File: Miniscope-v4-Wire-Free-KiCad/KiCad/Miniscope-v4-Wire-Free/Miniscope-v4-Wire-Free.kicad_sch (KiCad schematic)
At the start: 116 parts, among them J1 0475710001, J10 Conn_01x01, J11 Conn_01x01, J12 Conn_01x01, J14 Conn_01x01, J15 Conn_01x01, J16 Conn_01x01, J17 Conn_01x01, J18 Conn_01x01, J19 Conn_01x01, J2 Conn_01x04, J20 Conn_01x01, J21 Conn_01x01, J22 Conn_01x01, J23 Conn_01x01, J24 Conn_01x01, J25 Conn_01x01, J26 Conn_01x01, J27 Conn_01x01, J3 Conn_01x04, J4 Conn_01x01, J5 Conn_01x01, J6 Conn_01x01, J7 Conn_01x01, J8 Conn_01x01, J9 Conn_01x01, Q1 NTK3134NT1G, Q2 MMBT3904LP-7B, SW1 TL3780AF330QG, U1 LTC3554, U2 HV892, U3 LTC3218, U4 MAX13030EETE+BGA, U5 TSOP57438TT1, U6 ATSAMD51J20A-UUT-EFP, U7 NCP163AMX330TBG, U8 NOIP1SN0480A, U9 LMV321IDCKR, Y2 Crystal

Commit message: Update public repository
- Made copy to a public repository
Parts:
- removed C?: 1u, .Capacitor:C_0201_0603Metric_L, symbol .Device:C_Small
- R22: renamed from R?; footprint .Resistor:R_0201_0603Metric_ERJ_L -> Resistor:R_0201_0603Metric_ERJ_L

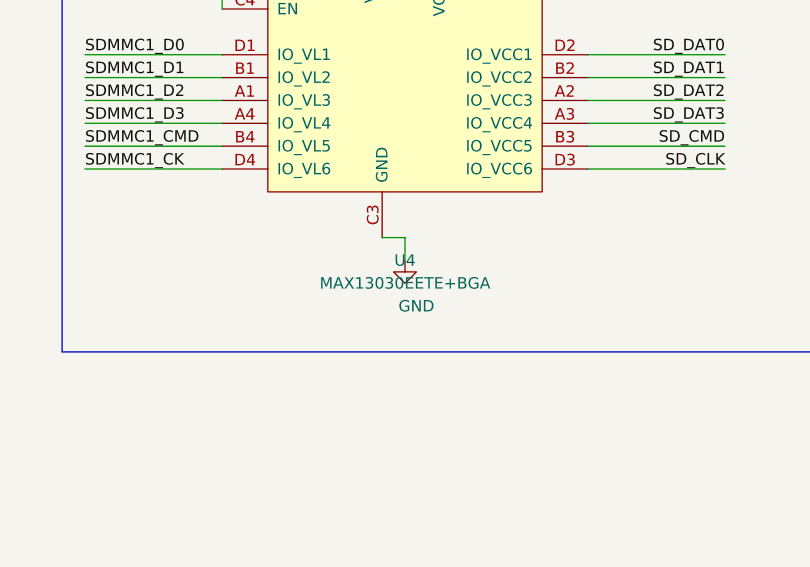
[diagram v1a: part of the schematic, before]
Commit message: Microchip Studio project reorganization, updates to the notebooks
- Reorganized the firmware repository. Now the project can be correctly reconfigured using Atmel Start and the clock settings is correct.

- Added a scan feature for the EWL. By setting a flag on the Set Parameters notebook the user can test different planes to check which one focuses better. More information on how to use this feature can be found soon on the Wire-Free wiki page.

- Added more information to the KiCad project for the batch assembly.

To do:

- Do a final cleaning of the firmware code. See if it's worth moving the ADMA and SDHC specific functions to a custom file
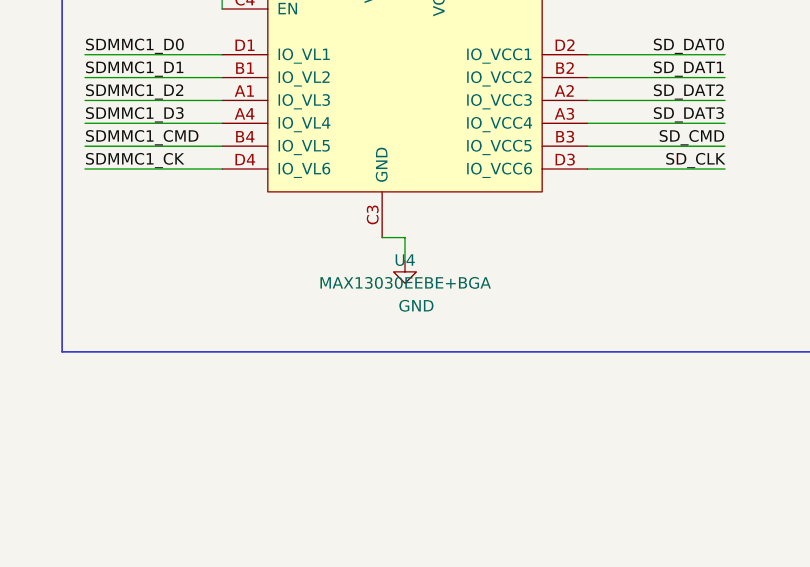
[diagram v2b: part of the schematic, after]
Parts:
- U4: value MAX13030EETE+BGA -> MAX13030EEBE+BGA
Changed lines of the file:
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@@
       (effects (font (size 1.27 1.27)))
     )
-    (property "Value" "MAX13030EETE+BGA" (at 473.71 336.55 0)
+    (property "Value" "MAX13030EEBE+BGA" (at 473.71 336.55 0)
       (effects (font (size 1.27 1.27)))
     )

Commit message: Fix to the PCB project
- Reverted the project to KiCAD 6 to avoid breaking microvias when moving to KiCAD 7 or 8
- SPI_CS now connected again

To do:

- Remove the asterisk on the microcontroller silk layer
- Add gerbers for the new PCB
- Discuss with Daniel which numbering version to use
- Add back the 3D models
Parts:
- removed R21: 47k5, .Resistor:R_0201_0603Metric_ERJ_L, symbol .Device:R_Small_US
- removed R22: 10K, Resistor:R_0201_0603Metric_ERJ_L, symbol .Device:R_Small_US
- added R?: 47k5, Custom:R_0201_0603Metric_ERJ_L, symbol Miniscope-v4-Wire-Free-rescue:R_Small_US-.Device
- added R?: 10K, Custom:R_0201_0603Metric_ERJ_L, symbol Miniscope-v4-Wire-Free-rescue:R_Small_US-.Device
- C1, C2, C26, C35, C50, C51, C52, C6, C7: symbol .Device:C_Small -> Miniscope-v4-Wire-Free-rescue:C_Small-.Device; Manufacturer_Name Murata -> (none); Manufacturer_Part_Number GRM155R60J106ME15D -> (none)
- C10, C19, C22, C23, C24, C25, C27, C28, C30, C38, C40, C41, C42, C43, C44, C45, C46, C47, C48, C49, C53, C9: symbol .Device:C_Small -> Miniscope-v4-Wire-Free-rescue:C_Small-.Device; Manufacturer_Name Murata -> (none); Manufacturer_Part_Number GRM033R61E104KE14J -> (none)
- C11, C12, C13, C15, C5: symbol .Device:C_Small -> Miniscope-v4-Wire-Free-rescue:C_Small-.Device; Manufacturer_Name Murata -> (none); Manufacturer_Part_Number GRM033R61A225KE47D -> (none)
- C14, C37: symbol .Device:C_Small -> Miniscope-v4-Wire-Free-rescue:C_Small-.Device; Manufacturer_Name Murata -> (none); Manufacturer_Part_Number GRM033R61A105ME15D -> (none)
- C16: symbol .Device:C_Small -> Miniscope-v4-Wire-Free-rescue:C_Small-.Device; Manufacturer_Name Murata -> (none); Manufacturer_Part_Number GCM188R72A472KA37D -> (none)
- C17, C29, C36: symbol .Device:C_Small -> Miniscope-v4-Wire-Free-rescue:C_Small-.Device; Manufacturer_Name Murata -> (none); Manufacturer_Part_Number GRM035R60J475ME15D -> (none)
- C18, C20: symbol .Device:C_Small -> Miniscope-v4-Wire-Free-rescue:C_Small-.Device; Manufacturer_Name Murata -> (none); Manufacturer_Part_Number GRM0335C1H220GA01D -> (none)
- C3, C4: symbol .Device:C_Small -> Miniscope-v4-Wire-Free-rescue:C_Small-.Device; Manufacturer_Name Murata -> (none); Manufacturer_Part_Number GRM0335C1H100FA01J -> (none)
- D1: value LXZ1-PB01 -> LXZ1-PR01; symbol .LED:LXZ1-PR01 -> Miniscope-v4-Wire-Free-rescue:LXZ1-PR01-.LED; Manufacturer_Name Lumileds -> (none); Manufacturer_Part_Number LXZ1-PB01 -> (none)
- D2, D3: symbol .Device:LED_Small_ALT -> Miniscope-v4-Wire-Free-rescue:LED_Small_ALT-.Device
- J1: symbol .Connector:0475710001 -> Miniscope-v4-Wire-Free-rescue:0475710001-.Connector; Manufacturer_Name Molex -> (none); Manufacturer_Part_Number 0475710001 -> (none)
- J10, J11, J12, J14, J15, J16, J17, J18, J19, J20, J21, J22, J23, J24, J25, J26, J27, J4, J5, J6, J7, J8, J9: Manufacturer_Name DNL -> (none); Manufacturer_Part_Number DNL -> (none); PN DNL -> (none)
- J2, J3: Manufacturer_Name DNL -> (none); Manufacturer_Part_Number DNL -> (none)
- L1, L5: symbol .Device:L_Small -> Miniscope-v4-Wire-Free-rescue:L_Small-.Device; Manufacturer_Name TDK -> (none); Manufacturer_Part_Number MLZ1608N100LT000 -> (none); PN MLZ1608N100LT00 -> (none)
- L2: symbol .Device:L_Small -> Miniscope-v4-Wire-Free-rescue:L_Small-.Device; Manufacturer_Name Abracon -> (none); Manufacturer_Part_Number ASMCI-0805-4R7M-T -> (none); PN ASMCI-0805-4R7M-T -> (none)
- L3: value BLM18PG471SN1D -> L_Small; symbol .Device:L_Small -> Miniscope-v4-Wire-Free-rescue:L_Small-.Device; Manufacturer_Name Murata -> (none); Manufacturer_Part_Number BLM18PG471SN1D -> (none)
- L4: symbol .Device:L_Small -> Miniscope-v4-Wire-Free-rescue:L_Small-.Device; Manufacturer_Name Murata -> (none); Manufacturer_Part_Number BLM18PG471SN1D -> (none)
- Q1: symbol .Transistor:NTK3134NT1G -> Miniscope-v4-Wire-Free-rescue:NTK3134NT1G-.Transistor
- Q2: symbol .Transistor:MMBT3904LP-7B -> Miniscope-v4-Wire-Free-rescue:MMBT3904LP-7B-.Transistor; Manufacturer_Name Diodes Incorporated -> (none); Manufacturer_Part_Number MMBT3904LP-7B -> (none)
- R1, R17: symbol .Device:R_Small_US -> Miniscope-v4-Wire-Free-rescue:R_Small_US-.Device; Manufacturer_Name Vishay Dale -> (none); Manufacturer_Part_Number CRCW020124K9FNED -> (none)
- R10: symbol .Device:R_Small_US -> Miniscope-v4-Wire-Free-rescue:R_Small_US-.Device; Manufacturer_Name Vishay Dale -> (none); Manufacturer_Part_Number CRCW02012K00FNED -> (none)
- R11, R19: symbol .Device:R_Small_US -> Miniscope-v4-Wire-Free-rescue:R_Small_US-.Device; Manufacturer_Name Vishay Dale -> (none); Manufacturer_Part_Number CRCW02011K00FKED -> (none)
- R12: symbol .Device:R_Small_US -> Miniscope-v4-Wire-Free-rescue:R_Small_US-.Device; Manufacturer_Name DNL -> (none); Manufacturer_Part_Number DNL -> (none)
- R13: symbol .Device:R_Small_US -> Miniscope-v4-Wire-Free-rescue:R_Small_US-.Device; Manufacturer_Name Panasonic -> (none); Manufacturer_Part_Number ERJ-1GNF4023C -> (none)
- R14, R16, R20: symbol .Device:R_Small_US -> Miniscope-v4-Wire-Free-rescue:R_Small_US-.Device; Manufacturer_Name Panasonic -> (none); Manufacturer_Part_Number ERJ-1GNF1003C -> (none)
- R15: symbol .Device:R_Small_US -> Miniscope-v4-Wire-Free-rescue:R_Small_US-.Device; Manufacturer_Name Panasonic -> (none); Manufacturer_Part_Number ERJ-1GNF3742C -> (none)
- R18: symbol .Device:R_Small_US -> Miniscope-v4-Wire-Free-rescue:R_Small_US-.Device
- R2: value R_Small_US -> 1K8; symbol .Device:R_Small_US -> Miniscope-v4-Wire-Free-rescue:R_Small_US-.Device
- R3: symbol .Device:R_Small_US -> Miniscope-v4-Wire-Free-rescue:R_Small_US-.Device; Manufacturer_Name Vishay Dale -> (none); Manufacturer_Part_Number CRCW02011M27FNED -> (none)
- R4: symbol .Device:R_Small_US -> Miniscope-v4-Wire-Free-rescue:R_Small_US-.Device; Manufacturer_Name Vishay Dale -> (none); Manufacturer_Part_Number CRCW02012M05FNED -> (none)
- R5: symbol .Device:R_Small_US -> Miniscope-v4-Wire-Free-rescue:R_Small_US-.Device; Manufacturer_Name Vishay Dale -> (none); Manufacturer_Part_Number CRCW02011M00FNED -> (none)
- R6: symbol .Device:R_Small_US -> Miniscope-v4-Wire-Free-rescue:R_Small_US-.Device; Manufacturer_Name Vishay Dale -> (none); Manufacturer_Part_Number CRCW0201649KFNED -> (none)
- R7, R8: symbol .Device:R_Small_US -> Miniscope-v4-Wire-Free-rescue:R_Small_US-.Device; Manufacturer_Name Panasonic -> (none); Manufacturer_Part_Number ERJ-1GNF2201C -> (none)
- R9: symbol .Device:R_Small_US -> Miniscope-v4-Wire-Free-rescue:R_Small_US-.Device; Manufacturer_Name Vishay Dale -> (none); Manufacturer_Part_Number CRCW02018K20FKED -> (none)
- SW1: Manufacturer_Name E-Switch -> (none); Manufacturer_Part_Number TL3780AF330QG -> (none)
- U1: Manufacturer_Name Analog Devices Inc. -> (none); Manufacturer_Part_Number LTC3554EUD#PBF -> (none)
- U2: Manufacturer_Name Microchip -> (none); Manufacturer_Part_Number HV892K7-G -> (none)
- U3: symbol .Driver_LED:LTC3218 -> Miniscope-v4-Wire-Free-rescue:LTC3218-.Driver_LED; Manufacturer_Name Analog Devices Inc. -> (none); Manufacturer_Part_Number LTC3218 -> (none)
- U4: value MAX13030EEBE+BGA -> MAX13030EETE+BGA; Manufacturer_Name Maxim Integrated -> (none); Manufacturer_Part_Number MAX13030EETE+ -> (none)
- U5: symbol .IR_Receiver:TSOP57438TT1 -> Miniscope-v4-Wire-Free-rescue:TSOP57438TT1-.IR_Receiver; Manufacturer_Name Vishay Semiconductor Opto Division -> (none); Manufacturer_Part_Number TSOP57438TT1 -> (none)
- U6: Manufacturer_Name Microchip -> (none); Manufacturer_Part_Number ATSAMD51J20A-UUT-EFP -> (none)
- U7: symbol .Regulator_Linear:MCP1711 -> Miniscope-v4-Wire-Free-rescue:MCP1711-.Regulator_Linear; Manufacturer_Name onsemi -> (none); Manufacturer_Part_Number NCP163AMX330TBG -> (none)
- U8: symbol .Image_Sensor:NOIP1SN0480A -> Miniscope-v4-Wire-Free-rescue:NOIP1SN0480A-.Image_Sensor; Manufacturer_Name onsemi -> (none); Manufacturer_Part_Number NOIP1SN0480A-STI1 -> (none)
- U9: symbol .Opamp:LMV321IDCKR -> Miniscope-v4-Wire-Free-rescue:LMV321IDCKR-.Opamp
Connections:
- net +1V8: now also R?.1
- net GND: now also R?.2
- net nRESET: now also R?.2
- net at U8.E1 (IBIAS_MASTER): now also R?.1
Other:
- note added: "ATSAMD51J20A Microcontroller"
- note added: "Battery connector"
- note added: "Crystal resonator"
- note added: "Fix for non functional internal pull-up on the Reset pin. See section 2.6.2 of the errata for more details "SAM D5X E5X Family Silicon Errata and Data-Sheet Clarification 80000748F""
- note added: "Status LED"
- note removed: "Added missing 47k5 resistor"
- note removed: "Changed enable to 3V3 to comply better with power on sequence"
- note removed: "MCU"
- note removed: "RC circuit to run the Wire-free without the debugger."
- moved on the sheet: C10, C11, C12, C13, C14, C15, C16, C17, C18, C20, C9, D1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

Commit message: Added part numbers to all the components.
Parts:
- C1, C2, C26, C35, C50, C51, C52, C6, C7: MPN (none) -> CL05A106MP5NUNC; OEPS PN (none) -> OEPS010038
- C10, C19, C22, C23, C24, C25, C27, C28, C30, C38, C40, C41, C42, C43, C44, C45, C46, C47, C48, C49, C53, C9: MPN (none) -> GRM033R61E104KE14J; OEPS PN (none) -> OEPS010035
- C11, C12, C13, C15, C5: MPN (none) -> CM03X5R225M10AH; OEPS PN (none) -> OEPS010042
- C14, C37: MPN (none) -> CL03A105MO3NRNH; OEPS PN (none) -> OEPS010036
- C16: MPN (none) -> 885012206112; OEPS PN (none) -> OEPS010014
- C17, C29, C36: MPN (none) -> GRM035R60J475ME15D; OEPS PN (none) -> OEPS010065
- C18, C20: MPN (none) -> GRM0335C1H270GA01D; OEPS PN (none) -> OEPS010029
- C3, C4: MPN (none) -> GRM0335C1H100JA01J; OEPS PN (none) -> OEPS010060
- D1: MPN (none) -> LXZ1-PR01; OEPS PN (none) -> OEPS030021
- D2, D3: value LED_Small_ALT -> LTST-C191KEKT; MPN (none) -> LTST-C191KEKT; OEPS PN (none) -> OEPS030029
- J1: MPN (none) -> 0475710001; OEPS PN (none) -> OEPS070078
- J10, J11, J12, J14, J15, J16, J17, J18, J19, J20, J21, J22, J23, J24, J25, J26, J27, J4, J5, J6, J7, J8, J9: value Conn_01x01 -> DNP; MPN (none) -> n.a.; OEPS PN (none) -> n.a.
- J2: value Conn_01x04 -> DNP; MPN (none) -> n.a.; OEPS PN (none) -> n.a.
- J3: MPN (none) -> FH19C-4S-0.5SH(10); OEPS PN (none) -> OEPS070077
- L1, L5: MPN (none) -> MLZ1608N100LT000; OEPS PN (none) -> OEPS040021
- L2: MPN (none) -> MLP2012S4R7MT0S1; OEPS PN (none) -> OEPS040022
- L3: value L_Small -> BLM18PG471SN1D; MPN (none) -> BLM18PG471SN1D; OEPS PN (none) -> OEPS040014
- L4: MPN (none) -> BLM18PG471SN1D; OEPS PN (none) -> OEPS040014
- Q1: MPN (none) -> NTK3134NT1G; OEPS PN (none) -> OEPS060015
- Q2: MPN (none) -> MMBT3904LP-7B; OEPS PN (none) -> OEPS060014
- R1, R17: value 25K -> 24.9k; MPN (none) -> CRCW020124K9FNED; OEPS PN (none) -> OEPS020105
- R10: MPN (none) -> RC0201FR-072KL; OEPS PN (none) -> OEPS020067
- R11, R19: MPN (none) -> RC0201FR-071KL; OEPS PN (none) -> OEPS020065
- R12: value DNL -> DNP; MPN (none) -> n.a.; OEPS PN (none) -> n.a.
- R13: value 400K -> 402k; MPN (none) -> ERJ-1GNF4023C; OEPS PN (none) -> OEPS020112
- R14, R16, R20: MPN (none) -> ERJ-1GNF1003C; OEPS PN (none) -> OEPS020072
- R15: value 37K -> 37.4k; MPN (none) -> ERJ-1GNF3742C; OEPS PN (none) -> OEPS020113
- R18: value R_Small_US -> 1k8; MPN (none) -> ERJ-1GNF1801C; OEPS PN (none) -> OEPS020114
- R2: MPN (none) -> ERJ-1GNF1801C; OEPS PN (none) -> OEPS020074
- R21: renamed from R?; MPN (none) -> ERJ-1GNF1002C; OEPS PN (none) -> OEPS020071
- R22: renamed from R?; MPN (none) -> ERJ-1GNF4752C; OEPS PN (none) -> OEPS020075
- R3: value 1.25M -> 1.27M; MPN (none) -> CRCW02011M27FNED; OEPS PN (none) -> OEPS020106
- R4: MPN (none) -> CRCW02012M05FNED; OEPS PN (none) -> OEPS020107
- R5: MPN (none) -> CRCW02011M00FNED; OEPS PN (none) -> OEPS020108
- R6: value 649K -> 649k; MPN (none) -> RC0201FR-07649KL; OEPS PN (none) -> OEPS020109
- R7, R8: value 2.2K -> 2.2k; MPN (none) -> RC0201FR-072K2L; OEPS PN (none) -> OEPS020110
- R9: value 8.2K -> 8.2k; MPN (none) -> ERJ-1GNF8201C; OEPS PN (none) -> OEPS020111
- SW1: MPN (none) -> TL3780AF330QG; OEPS PN (none) -> OEPS100050
- U1: MPN (none) -> LTC3554EUD#PBF; OEPS PN (none) -> OEPS080113
- U2: MPN (none) -> HV892K7-G; OEPS PN (none) -> OEPS080111
- U3: MPN (none) -> LTC3218EDDB#TRMPBF; OEPS PN (none) -> OEPS080069
- U4: value MAX13030EETE+BGA -> MAX13030EEBE+T; MPN (none) -> MAX13030EEBE+T; OEPS PN (none) -> OEPS080114
- U5: MPN (none) -> TSOP57438TT1; OEPS PN (none) -> OEPS080117
- U6: value ATSAMD51J20A-UUT-EFP -> ATSAMD51J20A; MPN (none) -> ATSAMD51J20A-UUT-EFP; OEPS PN (none) -> OEPS080115
- U7: MPN (none) -> NCP163AMX330TBG; OEPS PN (none) -> OEPS080076
- U8: value NOIP1SN0480A -> NOIP1SP0480A-STI; MPN (none) -> NOIP1SP0480A-STI; OEPS PN (none) -> OEPS080071
- U9: MPN (none) -> LMV321IDCKR; OEPS PN (none) -> OEPS080068
- Y2: value Crystal -> XTAL 32.7680KHZ; MPN (none) -> 9HT11-32.768KBZF-T; OEPS PN (none) -> OEPS100051
